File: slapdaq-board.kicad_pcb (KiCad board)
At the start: 4 copper layers, 69 parts, among them J1 Higher Screw Terminals, J2 Lower Screw Terminals, J3 USB-C, Q1 BSS84, U1 LM2675M-3.3, U2 LM2675M-5, U3 ESP32-S3, U4 DT1042-04SO-7, U5 REF3333, U6 ADS1261, U7 MAX31856

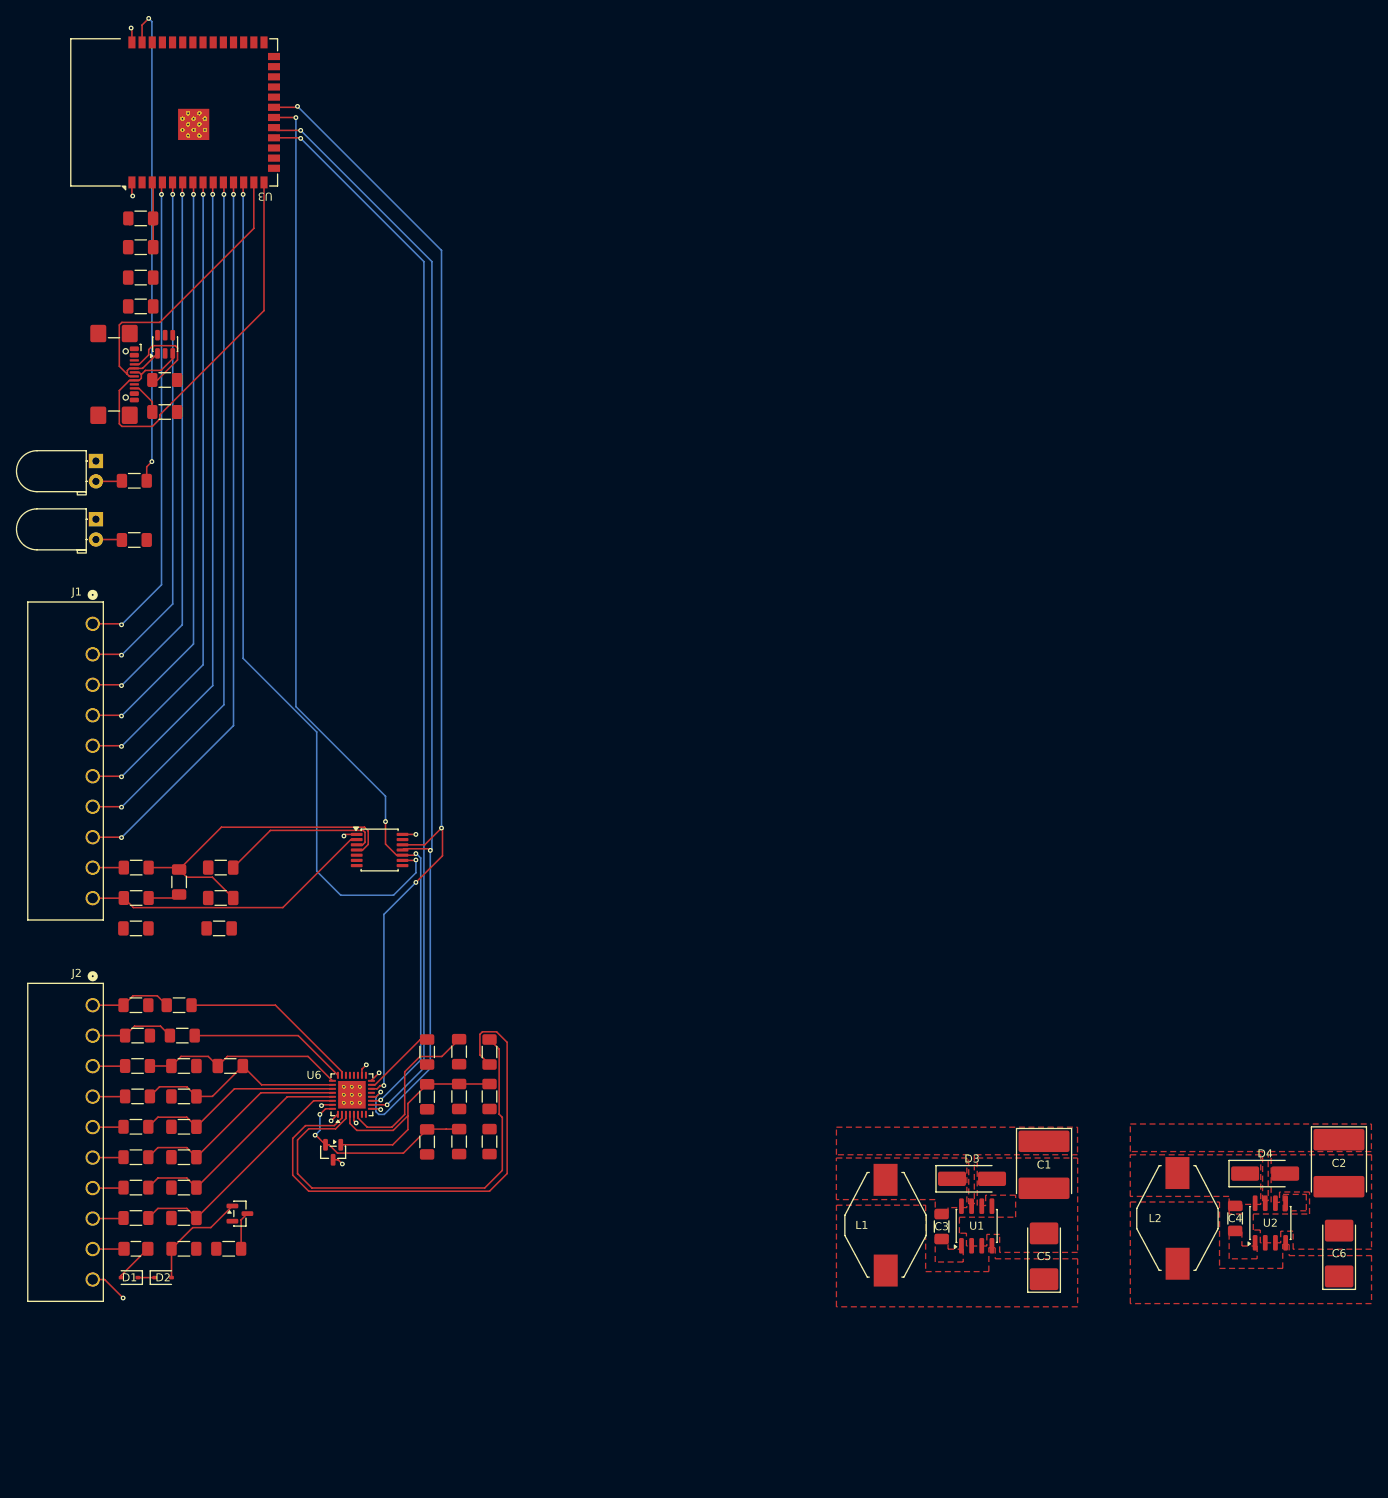
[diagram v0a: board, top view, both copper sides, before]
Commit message: implemented PCB feedback from meeting
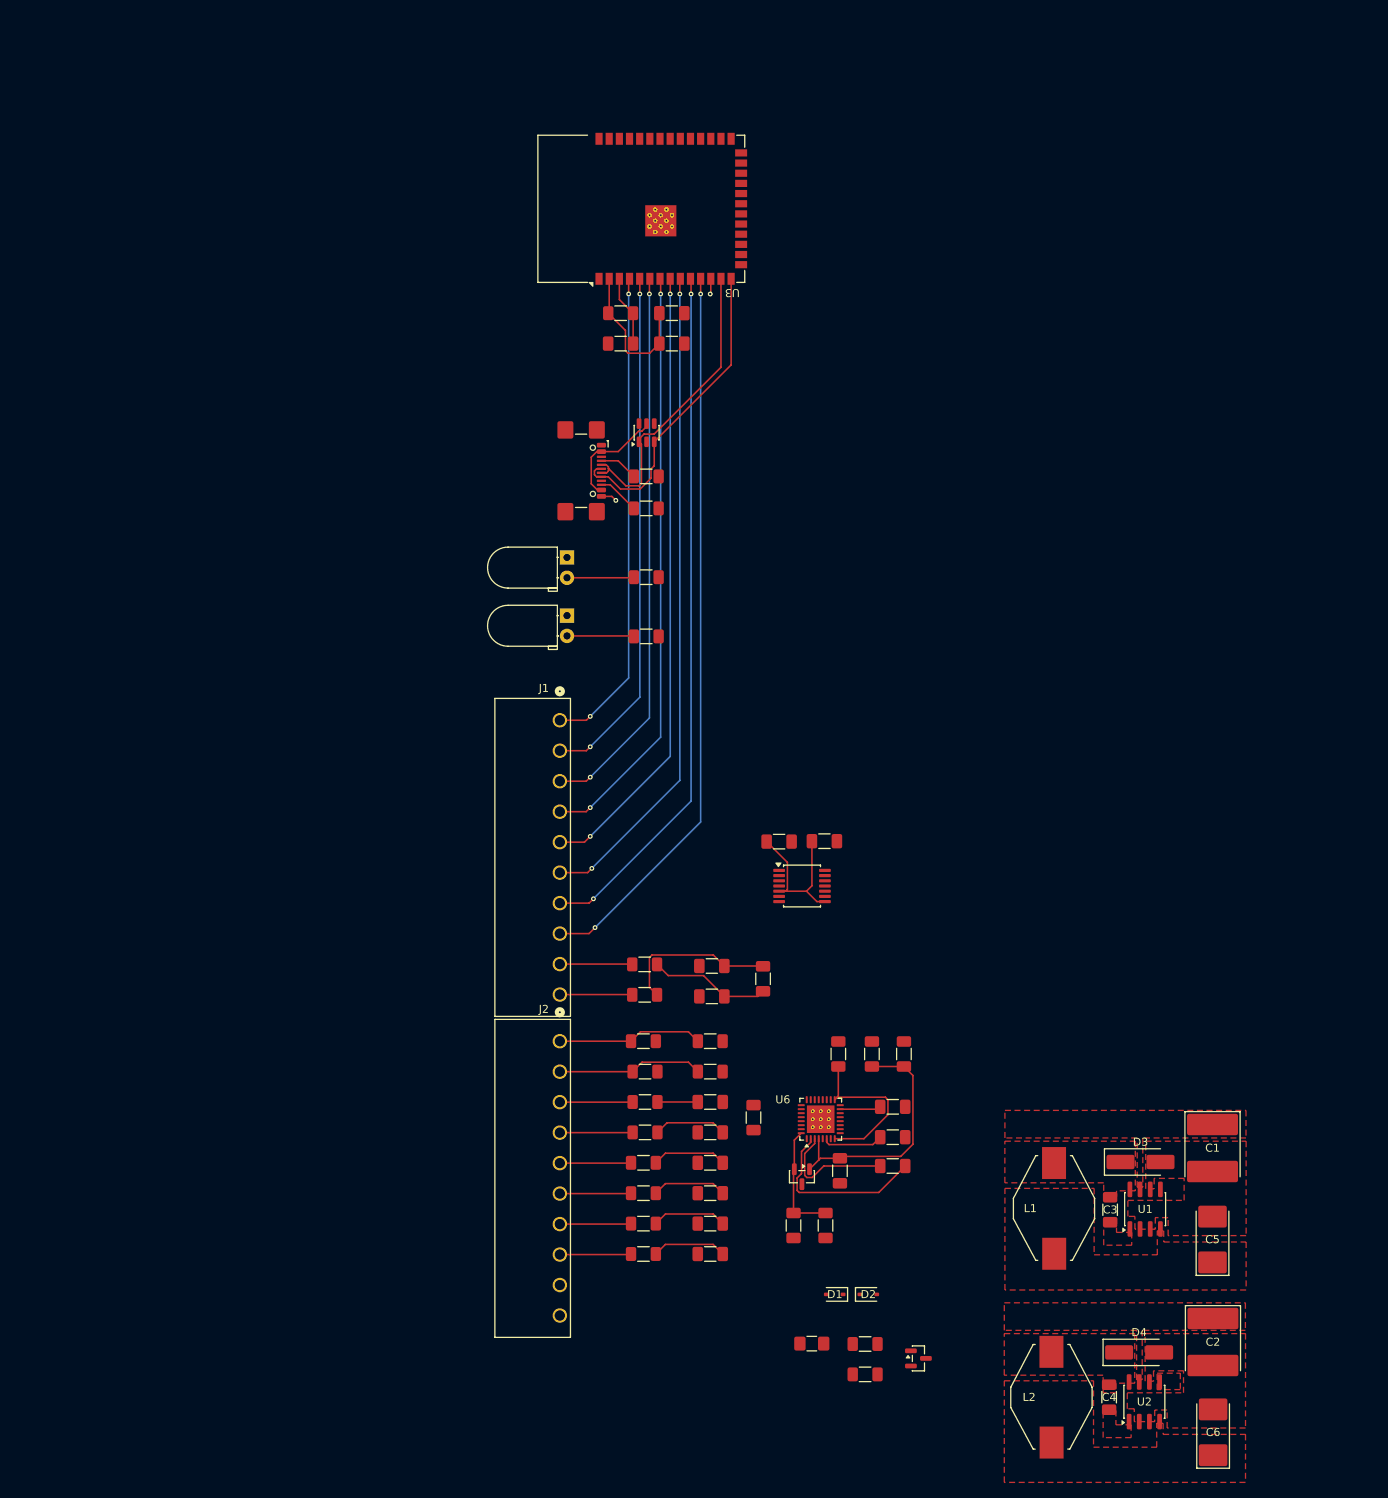
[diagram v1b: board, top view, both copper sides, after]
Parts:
- moved D2 88.2 mm to (141.6, 196.5)
- moved D1 88.2 mm to (137.3, 196.5)
- moved C29 86.8 mm to (136.1, 139.8)
- moved Q1 86.7 mm to (147.8, 204.5)
- moved R1 86.0 mm to (141.2, 202.7), turned to 180 degrees
- moved F1 85.3 mm to (134.5, 202.7)
- moved R2 81.1 mm to (141.2, 206.5)
- moved C28 74.0 mm to (128.4, 157.1), turned to 90 degrees
- moved C30 70.8 mm to (130.4, 139.9)
- moved C9 66.6 mm to (117.0, 77.7)
- moved R17 66.5 mm to (121.8, 164.8)
- moved C8 66.5 mm to (117.0, 73.8)
- moved R16 66.1 mm to (121.8, 168.7)
- moved C10 65.9 mm to (121.8, 176.2)
- moved C11 65.9 mm to (121.8, 172.4)
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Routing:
- net SPI_D: track 144.7 -> 0.00 mm, vias 3 -> 0
- net SPI_Q: track 143.4 -> 0.00 mm, vias 4 -> 0
- net SPI_CLK: track 137.0 -> 0.00 mm, vias 4 -> 0
- net CS0_ADC: track 134.4 -> 0.00 mm, vias 2 -> 0
- net CS1_THR: track 108.0 -> 1.93 mm, vias 2 -> 1
- net /MCU/WIFI_LED: track 61.6 -> 0.00 mm, vias 2 -> 0
- net +3.3V: track 0.02 -> 60.6 mm
- net Net-(U6-CAPP): track 65.6 -> 22.2 mm
- net Net-(U6-CAPN): track 56.2 -> 15.2 mm
- net TH-: track 37.0 -> 9.06 mm
- net Net-(U7-T+): track 41.6 -> 15.2 mm
- net Net-(U6-AIN9): track 22.7 -> 0.00 mm
- net Net-(U6-AIN2): track 30.1 -> 9.36 mm
- net Net-(U6-AIN7): track 25.6 -> 5.04 mm
- net Net-(U6-AIN8): track 20.0 -> 0.00 mm
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
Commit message: moved usb
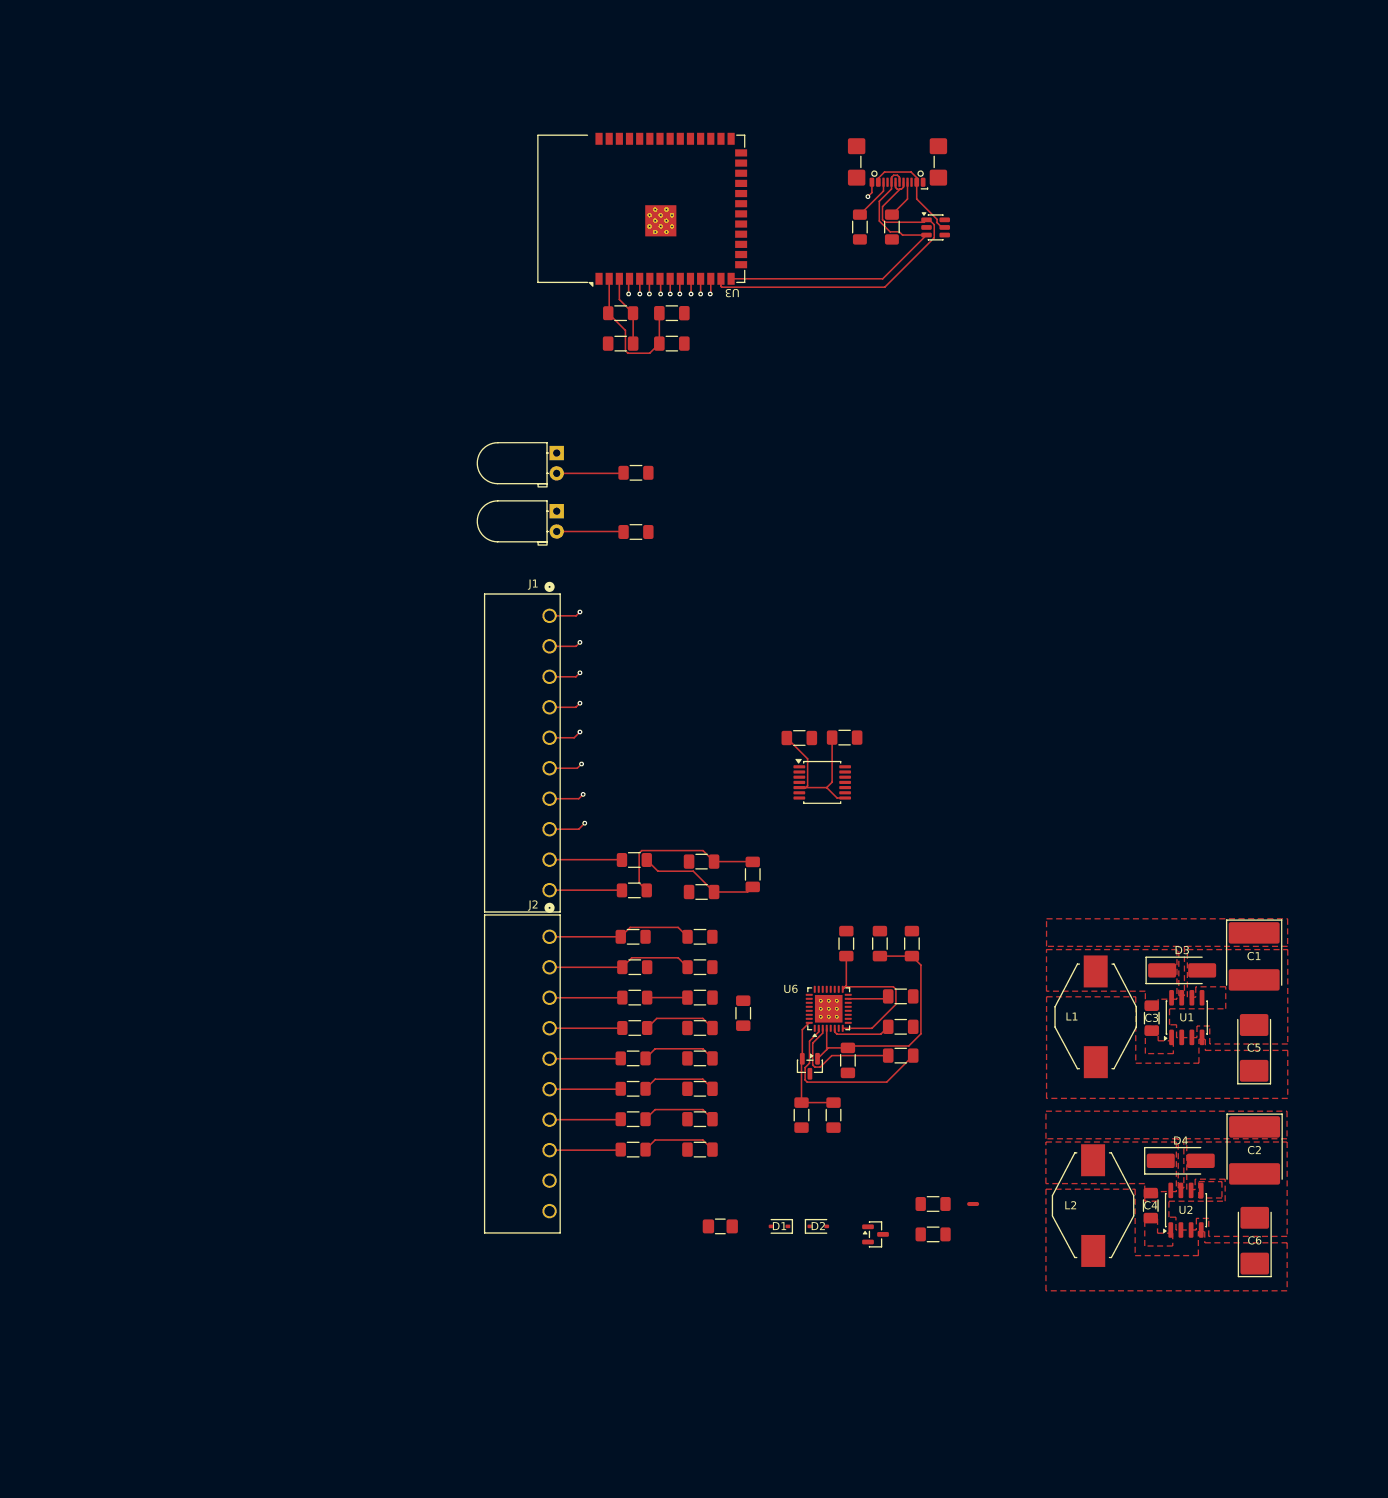
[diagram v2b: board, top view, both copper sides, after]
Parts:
- added NT1: NetTie_2, NetTie:NetTie-2_SMD_Pad0.5mm, F.Cu at (154.7, 185.2)
- moved J3 56.9 mm to (145.2, 53.8), turned to 180 degrees
- moved U4 44.3 mm to (150.0, 63.1), turned to 0 degrees
- moved R7 44.2 mm to (140.5, 63.1), turned to 90 degrees
- moved R6 43.8 mm to (144.5, 63.1), turned to 90 degrees
- moved C6 24.5 mm to (189.9, 189.8)
- moved U2 24.5 mm to (181.3, 186.0)
- moved L2 24.5 mm to (169.7, 185.4)
- moved U1 24.5 mm to (181.4, 161.9)
- moved C1 24.5 mm to (189.8, 154.2)
- moved C2 24.5 mm to (189.8, 178.5)
- moved C3 24.5 mm to (177.0, 162.0)
- moved C4 24.5 mm to (176.9, 185.4)
- moved C5 24.5 mm to (189.8, 165.7)
- moved D3 24.5 mm to (180.8, 156.0)
- moved D4 24.5 mm to (180.6, 179.8)
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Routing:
- net DIO6: track 87.0 -> 74.5 mm
- net DIO2: track 69.4 -> 56.9 mm
- net DIO0: track 60.7 -> 48.2 mm
- net DIO7: track 91.3 -> 78.8 mm
- net DIO5: track 82.5 -> 70.0 mm
- net DIO3: track 73.8 -> 61.3 mm
- net DIO4: track 77.9 -> 65.4 mm
- net DIO1: track 65.1 -> 52.6 mm
- net Net-(U3-USB_D-): track 38.3 -> 46.0 mm
- net Net-(U3-USB_D+): track 38.9 -> 41.2 mm

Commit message: moved LEDs over a little, did a sample edge cut, and some traces that i think could work
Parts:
- added REF**: MountingHole_3.5mm, MountingHole:MountingHole_3.5mm, F.Cu at (109.0, 190.4)
- added REF**: MountingHole_3.5mm, MountingHole:MountingHole_3.5mm, F.Cu at (182.8, 55.8)
- moved D6 4.40 mm to (102.7, 86.9)
- moved R5 4.40 mm to (112.6, 89.4)
- moved D5 2.80 mm to (102.6, 95.8)
- moved R4 2.80 mm to (112.5, 98.4)
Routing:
- net SPI_CLK: track 0.00 -> 121.1 mm, vias 0 -> 3
- net SPI_D: track 0.00 -> 117.4 mm, vias 0 -> 3
- net SPI_Q: track 0.00 -> 114.9 mm, vias 0 -> 3
- net CS0_ADC: track 0.00 -> 110.0 mm, vias 0 -> 2
- net CS1_THR: track 1.93 -> 72.0 mm
- net /MCU/WIFI_LED: track 0.00 -> 41.1 mm
- net TH-: track 9.06 -> 39.2 mm
- net +3.3V: track 60.6 -> 83.2 mm
- net +12V: track 0.00 -> 22.2 mm
- net Net-(U6-AIN2): track 9.36 -> 31.5 mm
- net Net-(U6-AIN3): track 9.36 -> 28.3 mm
- net Net-(U6-AIN7): track 5.04 -> 21.7 mm
- net Net-(U6-AIN4): track 9.36 -> 25.7 mm
- net Net-(U6-AIN9): track 0.00 -> 16.3 mm
- net Net-(U7-T+): track 15.2 -> 31.0 mm
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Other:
- board outline added: 96.2 x 145.8 mm
